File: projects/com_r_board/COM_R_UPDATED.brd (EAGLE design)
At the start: 90.2 x 95.9 mm, 18 parts, among them J1 0532610471, J2 53398-1271, J3 504050-0691, J4 ESQ-126-39-G-D, J5 ESQ-126-39-G-D, J6 G125-MS10605L3P

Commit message: COM_R revision 1. 12/8/2020
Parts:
- removed R1, R2, R4: 1k, rcl:M0805
- removed U$2: DF13-4P-1.25V, con-hirose-df13:DF13C-4P-1.25V
- added J7: 61300411121, SamacSys_Parts:HDRV4W95P0X254_1X4_1016X254X85
- added R3: TNPW080510K0BETY, TNPW080510K0BETY:RESC2012X55N
- added R6, R7: Y40621K00000Q0R, Y40621K00000Q0R:RESC2012X64N
- PWR_LED, RX_LED, TX_LED: value (none) -> HSMQ-C170-T0000; device led:CHIP-LED0805 -> SamacSys_Parts:LEDC2012X90N
- R5: value 10k -> Y40621K00000Q0R; device rcl:WSC01/2 -> Y40621K00000Q0R:RESC2012X64N
- moved R5 71.1 mm to (11.4, 5.08), turned to 0 degrees
- moved TX_LED 1.13 mm to (2.82, 8.40), turned to 0 degrees
- moved RX_LED 0.96 mm to (3.03, 11.8), turned to 0 degrees
- moved PWR_LED 0.74 mm to (3.07, 15.2), turned to 0 degrees
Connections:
- net PH_NEG renamed PH5_NEG
- net PH_POS renamed PH5_POS
- net PWMA renamed NEG_LEAD
- net PWMB renamed POS_LEAD
- net VCC/5V renamed 5V_BUS
- removed net N$7: PWR_LED.A, R4.1
- removed net VCC/3V3: C2.1, J2.11, J5.17, U$2.P$1, U$3.P$18, U$3.P$23, U$3.P$24, U$3.P$25, U$3.P$26, U$3.P$27, U$3.P$28
- new net 3V3_COM: C2.1, J2.11, J5.17, J7.2, U$3.P$18, U$3.P$23, U$3.P$24, U$3.P$25, U$3.P$26, U$3.P$27, U$3.P$28
- new net N$2: PWR_LED.2, R7.1
- net GND: now also J7.1, PWR_LED.1, R3.1, RX_LED.1, TX_LED.1; no longer PWR_LED.C, R5.1, RX_LED.C, TX_LED.C, U$2.P$2
- net N$1: now also R5.1, TX_LED.2; no longer R1.1, TX_LED.A
- net N$4: now also R6.1, RX_LED.2; no longer R2.1, RX_LED.A
- net PWR_LED: now also R7.2; no longer R4.2
- net RX_LED: now also R6.2; no longer R2.2
- net TX_LED: now also R5.2; no longer R1.2
- net UART_RX: now also J7.4; no longer U$2.P$4
- net UART_TX: now also J7.3, R3.2; no longer R5.2, U$2.P$3
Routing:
- net 3V3_COM: track 0.00 -> 200.7 mm, vias 0 -> 8
- net VCC/3V3: track 199.0 -> 0.00 mm, vias 8 -> 0
- net N$7: track 9.74 -> 0.00 mm
- net N$2: track 0.00 -> 7.46 mm, vias 1 -> 0
- net PWR_LED: track 39.7 -> 43.3 mm
- net 5V_BUS: track 86.9 -> 90.0 mm, vias 1 -> 2
- net UART_TX: track 143.2 -> 146.2 mm
- net RX_LED: track 30.2 -> 32.7 mm
- net TX_LED: track 28.6 -> 30.6 mm
- net N$4: track 9.61 -> 7.70 mm
- net GND: track 359.0 -> 360.9 mm, vias 13 -> 92
- net N$1: track 9.21 -> 8.05 mm
- net PH5_POS: track 69.3 -> 70.0 mm
- added copper zone on layer 15, net 3V3_COM
- removed copper zone on layer 15, net VCC/3V3
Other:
- board text added: "3V3_COM"
- board text added: "5V BUS"
- board text added: "C2"
- board text added: "COM_R Anika D. (12/3/2020)"
- board text added: "GND"
- board text added: "SHUTDOWN"
- board text added: "Solar Panel +Z H1"
- board text added: "UART_RX"
- board text added: "UART_TX"
- board text removed: "RADIO SHUTDOWN"
- board text removed: "Solar Panel +Z H2"

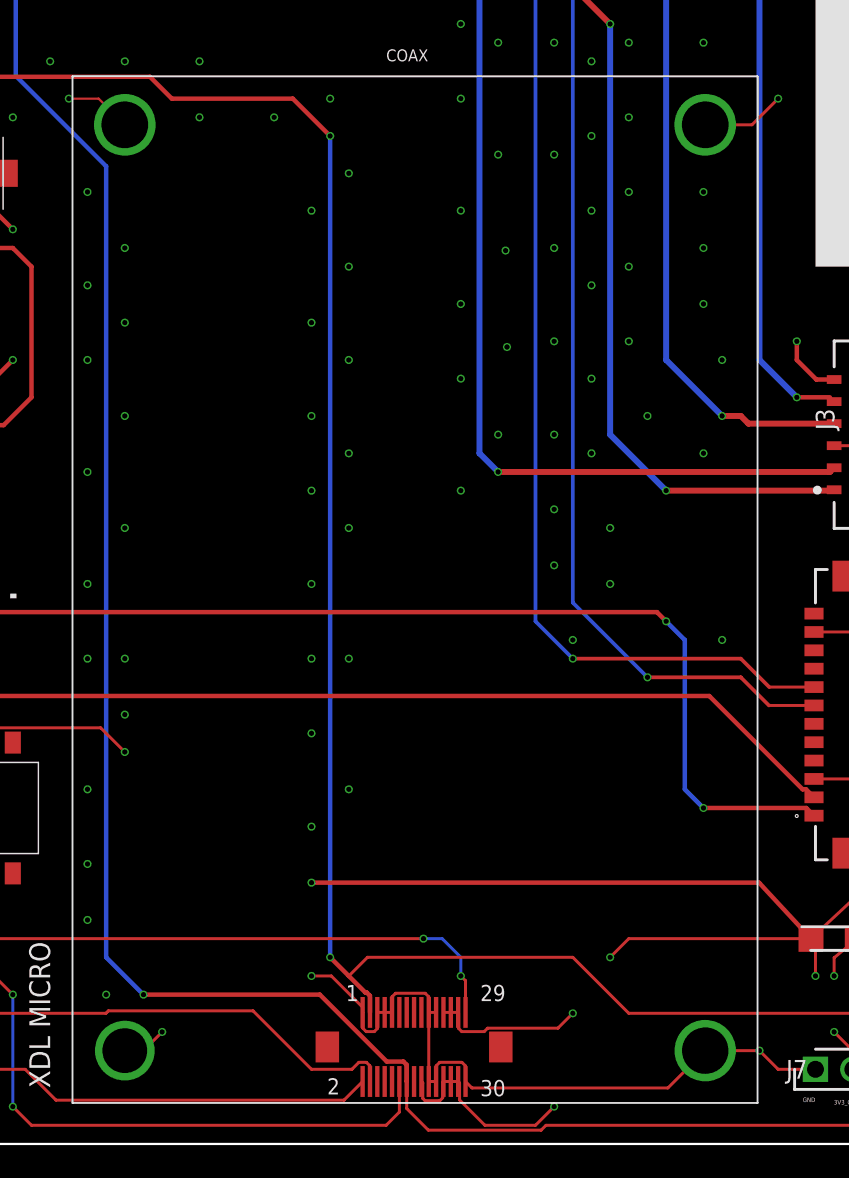
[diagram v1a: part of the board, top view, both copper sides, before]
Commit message: Fixed mounting hole dimensions
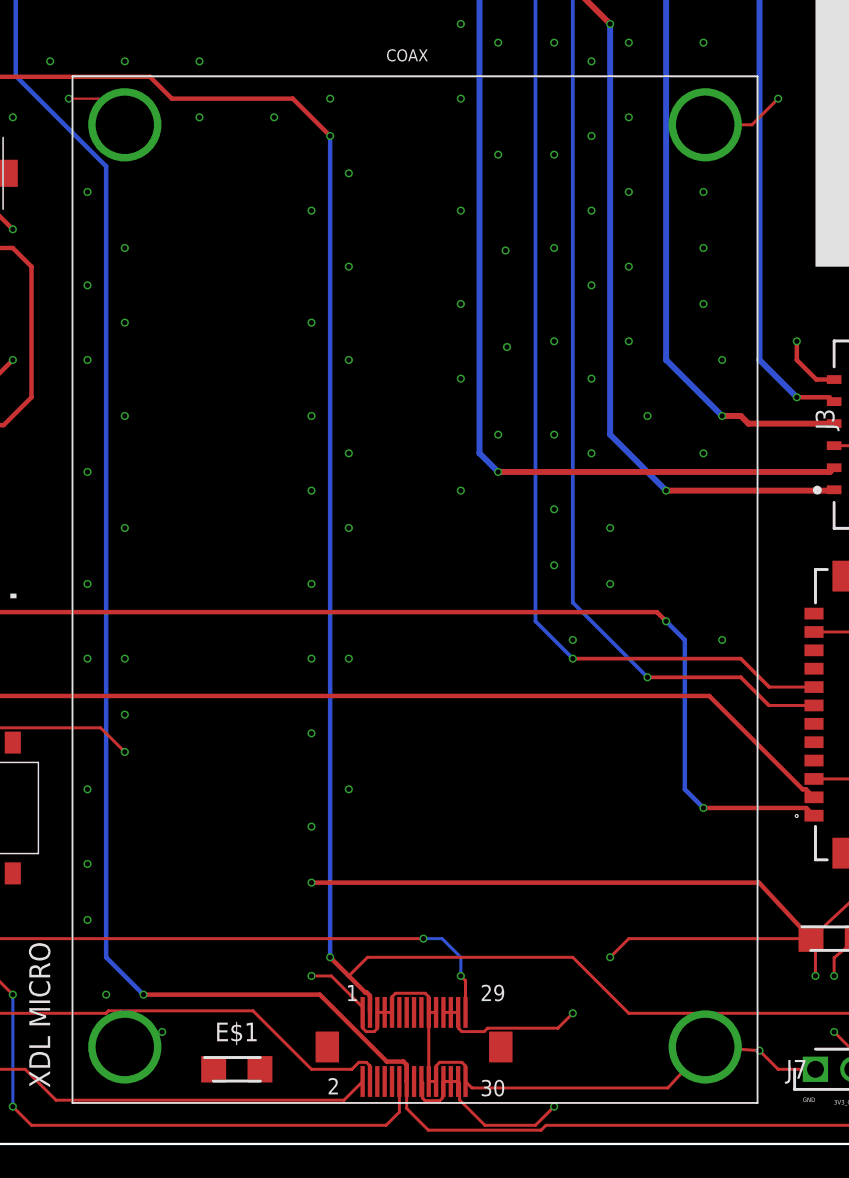
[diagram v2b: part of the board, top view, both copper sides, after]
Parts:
- added E$1: (no value), SamacSys_Parts:CAPPM3216X180N
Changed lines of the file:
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@@
 <attribute name="NAME" x="4.849459375" y="17.02346875" size="0.6096" layer="21" align="center"/>
+</element>
+<element name="E$1" library="SamacSys_Parts" package="CAPPM3216X180N" value="" x="33.02" y="5.08" smashed="yes">
+<attribute name="NAME" x="33.02" y="7.62" size="1.27" layer="25" align="center"/>
+<attribute name="VALUE" x="34.29" y="8.89" size="1.27" layer="27" align="center"/>
 </element>
 </elements>
@@
 <via x="27.94" y="7.62" extent="1-16" drill="0.35"/>
 <wire x1="27.94" y1="7.62" x2="26.67" y2="6.35" width="0.2032" layer="1"/>
-<wire x1="26.67" y1="6.35" x2="25.4" y2="6.35" width="0.2032" layer="1"/>
+<wire x1="26.67" y1="6.35" x2="25.4" y2="6.6" width="0.2032" layer="1"/>
 <wire x1="20.32" y1="77.47" x2="20.32" y2="74.93" width="0.1524" layer="2"/>
 <wire x1="20.32" y1="74.93" x2="20.32" y2="74.55406875" width="0.1524" layer="2"/>
@@
 <wire x1="73.66" y1="12.67" x2="75.235" y2="13.97" width="0.2032" layer="1"/>
 <wire x1="48.58" y1="4.25" x2="49.02" y2="3.81" width="0.2032" layer="1"/>
-<wire x1="62.35" y1="3.81" x2="64.89" y2="6.35" width="0.2032" layer="1"/>
+<wire x1="62.35" y1="3.81" x2="64.89" y2="6.6" width="0.2032" layer="1"/>
 <wire x1="49.02" y1="3.81" x2="62.35" y2="3.81" width="0.2032" layer="1"/>
 <via x="68.58" y="6.35" extent="1-16" drill="0.35"/>
-<wire x1="68.58" y1="6.35" x2="64.89" y2="6.35" width="0.2032" layer="1"/>
+<wire x1="68.58" y1="6.35" x2="64.89" y2="6.6" width="0.2032" layer="1"/>
 <wire x1="13.97" y1="61.74630625" x2="13.97" y2="64.19" width="0.2032" layer="1"/>
 <wire x1="80.01" y1="19.02" x2="75.235" y2="13.97" width="0.2032" layer="1"/>
@@
 <wire x1="2.077453125" y1="11.8469125" x2="2.077453125" y2="8.605615625" width="0.2032" layer="1"/>
 <wire x1="2.077453125" y1="8.605615625" x2="1.87435625" y2="8.40251875" width="0.2032" layer="1"/>
+<wire x1="64.77" y1="74.93" x2="64.77" y2="78.74" width="0" layer="19" extent="1-1"/>
+<wire x1="59.69" y1="74.93" x2="64.77" y2="74.93" width="0" layer="19" extent="1-1"/>
+<wire x1="57.15" y1="73.66" x2="59.69" y2="74.93" width="0" layer="19" extent="1-1"/>
+<wire x1="54.61" y1="74.93" x2="57.15" y2="73.66" width="0" layer="19" extent="1-1"/>
+<wire x1="50.8" y1="74.93" x2="54.61" y2="74.93" width="0" layer="19" extent="1-1"/>
+<wire x1="48.26" y1="76.2" x2="50.8" y2="74.93" width="0" layer="19" extent="1-1"/>
+<wire x1="58.42" y1="78.74" x2="59.69" y2="74.93" width="0" layer="19" extent="1-1"/>
+<wire x1="50.8" y1="80.01" x2="48.26" y2="76.2" width="0" layer="19" extent="1-1"/>
+<wire x1="59.69" y1="69.85" x2="57.15" y2="73.66" width="0" layer="19" extent="1-1"/>
+<wire x1="57.15" y1="68.58" x2="59.69" y2="69.85" width="0" layer="19" extent="1-1"/>
+<wire x1="54.61" y1="67.31" x2="57.15" y2="68.58" width="0" layer="19" extent="1-1"/>
+<wire x1="50.8" y1="67.31" x2="54.61" y2="67.31" width="0" layer="19" extent="1-1"/>
+<wire x1="59.69" y1="64.77" x2="57.15" y2="68.58" width="0" layer="19" extent="1-1"/>
+<wire x1="57.15" y1="63.5" x2="59.69" y2="64.77" width="0" layer="19" extent="1-1"/>
+<wire x1="54.61" y1="60.96" x2="57.15" y2="63.5" width="0" layer="19" extent="1-1"/>
+<wire x1="51.30573125" y1="60.785725" x2="54.61" y2="60.96" width="0" layer="19" extent="1-1"/>
+<wire x1="57.15" y1="58.42" x2="54.61" y2="60.96" width="0" layer="19" extent="1-1"/>
+<wire x1="59.69" y1="59.69" x2="57.15" y2="58.42" width="0" layer="19" extent="1-1"/>
+<wire x1="48.26" y1="63.5" x2="51.30573125" y2="60.785725" width="0" layer="19" extent="1-1"/>
+<wire x1="48.26" y1="71.12" x2="50.8" y2="74.93" width="0" layer="19" extent="1-1"/>
+<wire x1="59.69" y1="54.61" x2="57.15" y2="58.42" width="0" layer="19" extent="1-1"/>
+<wire x1="57.15" y1="52.07" x2="59.69" y2="54.61" width="0" layer="19" extent="1-1"/>
+<wire x1="54.61" y1="54.61" x2="57.15" y2="52.07" width="0" layer="19" extent="1-1"/>
+<wire x1="51.4026875" y1="54.22250625" x2="54.61" y2="54.61" width="0" layer="19" extent="1-1"/>
+<wire x1="48.26" y1="52.07" x2="51.4026875" y2="54.22250625" width="0" layer="19" extent="1-1"/>
+<wire x1="48.26" y1="57.15" x2="51.4026875" y2="54.22250625" width="0" layer="19" extent="1-1"/>
+<wire x1="60.96" y1="49.53" x2="57.15" y2="52.07" width="0" layer="19" extent="1-1"/>
+<wire x1="64.77" y1="46.99" x2="60.96" y2="49.53" width="0" layer="19" extent="1-1"/>
+<wire x1="54.61" y1="48.26" x2="57.15" y2="52.07" width="0" layer="19" extent="1-1"/>
+<wire x1="57.15" y1="46.99" x2="54.61" y2="48.26" width="0" layer="19" extent="1-1"/>
+<wire x1="50.8" y1="48.26" x2="54.61" y2="48.26" width="0" layer="19" extent="1-1"/>
+<wire x1="54.61" y1="43.18" x2="57.15" y2="46.99" width="0" layer="19" extent="1-1"/>
+<wire x1="54.61" y1="39.37" x2="54.61" y2="43.18" width="0" layer="19" extent="1-1"/>
+<wire x1="58.42" y1="41.91" x2="54.61" y2="43.18" width="0" layer="19" extent="1-1"/>
+<wire x1="58.42" y1="38.1" x2="58.42" y2="41.91" width="0" layer="19" extent="1-1"/>
+<wire x1="48.26" y1="44.45" x2="50.8" y2="48.26" width="0" layer="19" extent="1-1"/>
+<wire x1="55.88" y1="34.29" x2="58.42" y2="38.1" width="0" layer="19" extent="1-1"/>
+<wire x1="64.77" y1="64.77" x2="59.69" y2="64.77" width="0" layer="19" extent="1-1"/>
+<wire x1="64.77" y1="60.96" x2="64.77" y2="64.77" width="0" layer="19" extent="1-1"/>
+<wire x1="64.77" y1="57.15" x2="64.77" y2="60.96" width="0" layer="19" extent="1-1"/>
+<wire x1="66.04" y1="53.34" x2="64.77" y2="57.15" width="0" layer="19" extent="1-1"/>
+<wire x1="64.89" y1="69.34" x2="64.77" y2="64.77" width="0" layer="19" extent="1-1"/>
+<wire x1="25.4" y1="29.21" x2="25.4" y2="26.67" width="0" layer="19" extent="1-1"/>
+<wire x1="20.32" y1="73.66" x2="21.59" y2="71.12" width="0" layer="19" extent="1-1"/>
+<wire x1="22.86" y1="24.13" x2="25.4" y2="26.67" width="0" layer="19" extent="1-1"/>
+<wire x1="24.13" y1="10.16" x2="25.4" y2="6.6" width="0" layer="19" extent="1-1"/>
+<wire x1="25.4" y1="33.02" x2="25.4" y2="29.21" width="0" layer="19" extent="1-1"/>
+<wire x1="22.86" y1="33.02" x2="25.4" y2="33.02" width="0" layer="19" extent="1-1"/>
+<wire x1="17.78" y1="69.85" x2="21.59" y2="71.12" width="0" layer="19" extent="1-1"/>
+<wire x1="25.4" y1="73.66" x2="25.4" y2="69.34" width="0" layer="19" extent="1-1"/>
+<wire x1="30.48" y1="73.66" x2="25.4" y2="73.66" width="0" layer="19" extent="1-1"/>
+<wire x1="30.48" y1="69.85" x2="30.48" y2="73.66" width="0" layer="19" extent="1-1"/>
+<wire x1="35.56" y1="69.85" x2="30.48" y2="69.85" width="0" layer="19" extent="1-1"/>
+<wire x1="39.37" y1="71.12" x2="35.56" y2="69.85" width="0" layer="19" extent="1-1"/>
+<wire x1="22.86" y1="38.1" x2="22.86" y2="33.02" width="0" layer="19" extent="1-1"/>
+<wire x1="25.4" y1="41.91" x2="22.86" y2="38.1" width="0" layer="19" extent="1-1"/>
+<wire x1="22.86" y1="45.72" x2="25.4" y2="41.91" width="0" layer="19" extent="1-1"/>
+<wire x1="25.4" y1="49.53" x2="22.86" y2="45.72" width="0" layer="19" extent="1-1"/>
+<wire x1="22.86" y1="53.34" x2="25.4" y2="49.53" width="0" layer="19" extent="1-1"/>
+<wire x1="25.4" y1="55.88" x2="22.86" y2="53.34" width="0" layer="19" extent="1-1"/>
+<wire x1="22.86" y1="58.42" x2="25.4" y2="55.88" width="0" layer="19" extent="1-1"/>
+<wire x1="25.4" y1="60.96" x2="22.86" y2="58.42" width="0" layer="19" extent="1-1"/>
+<wire x1="22.86" y1="64.77" x2="25.4" y2="60.96" width="0" layer="19" extent="1-1"/>
+<wire x1="22.86" y1="19.05" x2="22.86" y2="24.13" width="0" layer="19" extent="1-1"/>
+<wire x1="22.86" y1="15.24" x2="22.86" y2="19.05" width="0" layer="19" extent="1-1"/>
+<wire x1="40.64" y1="66.04" x2="39.37" y2="71.12" width="0" layer="19" extent="1-1"/>
+<wire x1="38.1" y1="63.5" x2="40.64" y2="66.04" width="0" layer="19" extent="1-1"/>
+<wire x1="40.64" y1="59.69" x2="38.1" y2="63.5" width="0" layer="19" extent="1-1"/>
+<wire x1="38.1" y1="55.88" x2="40.64" y2="59.69" width="0" layer="19" extent="1-1"/>
+<wire x1="40.64" y1="53.34" x2="38.1" y2="55.88" width="0" layer="19" extent="1-1"/>
+<wire x1="38.1" y1="49.53" x2="40.64" y2="53.34" width="0" layer="19" extent="1-1"/>
+<wire x1="40.64" y1="46.99" x2="38.1" y2="49.53" width="0" layer="19" extent="1-1"/>
+<wire x1="38.1" y1="44.45" x2="40.64" y2="46.99" width="0" layer="19" extent="1-1"/>
+<wire x1="40.64" y1="41.91" x2="38.1" y2="44.45" width="0" layer="19" extent="1-1"/>
+<wire x1="38.1" y1="38.1" x2="40.64" y2="41.91" width="0" layer="19" extent="1-1"/>
+<wire x1="38.1" y1="33.02" x2="38.1" y2="38.1" width="0" layer="19" extent="1-1"/>
+<wire x1="40.64" y1="33.02" x2="38.1" y2="33.02" width="0" layer="19" extent="1-1"/>
+<wire x1="38.1" y1="27.94" x2="38.1" y2="33.02" width="0" layer="19" extent="1-1"/>
+<wire x1="40.64" y1="24.13" x2="38.1" y2="27.94" width="0" layer="19" extent="1-1"/>
+<wire x1="38.1" y1="21.59" x2="40.64" y2="24.13" width="0" layer="19" extent="1-1"/>
+<wire x1="66.04" y1="34.29" x2="58.42" y2="38.1" width="0" layer="19" extent="1-1"/>
 </signal>
 <signal name="N$4">
